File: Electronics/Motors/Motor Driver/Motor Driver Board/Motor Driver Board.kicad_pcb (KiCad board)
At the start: 4 copper layers, 102 x 75 mm, 158 parts, among them IC201 TPS563202DRLR, IC202 TPS563202DRLR, IC301 TJA1057GT/3, IC302 STM32H723ZGT6, J201 Conn_01x02_Pin, J202 Screw_Terminal_01x02, J203 Conn_01x02_Pin, J204 Conn_01x02_Pin, J301 TC2030, J302 Screw_Terminal_01x03, J303 TYPE-C-31-M-12, J401 XT60PW-F, J402 XT60PW-F, J403 XT60PW-M, J404 XT60PW-F, J405 XT60-M-Vertical, J406 Conn_01x05, J407 Conn_01x05, J408 Conn_01x05, Q201 DMP3028LFDE, SW301 SW_DIP_x02, T401 NVMFS4C05NT1G, T402 NVMFS4C05NT1G, T403 NVMFS4C05NT1G, T404 NVMFS4C05NT1G, T405 NVMFS4C05NT1G, T406 NVMFS4C05NT1G, T407 NVMFS4C05NT1G, T408 NVMFS4C05NT1G, T409 NVMFS4C05NT1G, T410 NVMFS4C05NT1G, T411 NVMFS4C05NT1G, T412 NVMFS4C05NT1G, U302 LSM6DS3, U303 USBLC6-4SC6-ES, U401 DRV8701ERGER, U402 DRV8701ERGER, U403 DRV8701ERGER, X301 25MHz_Clock, X302 32.768kHz_Clock

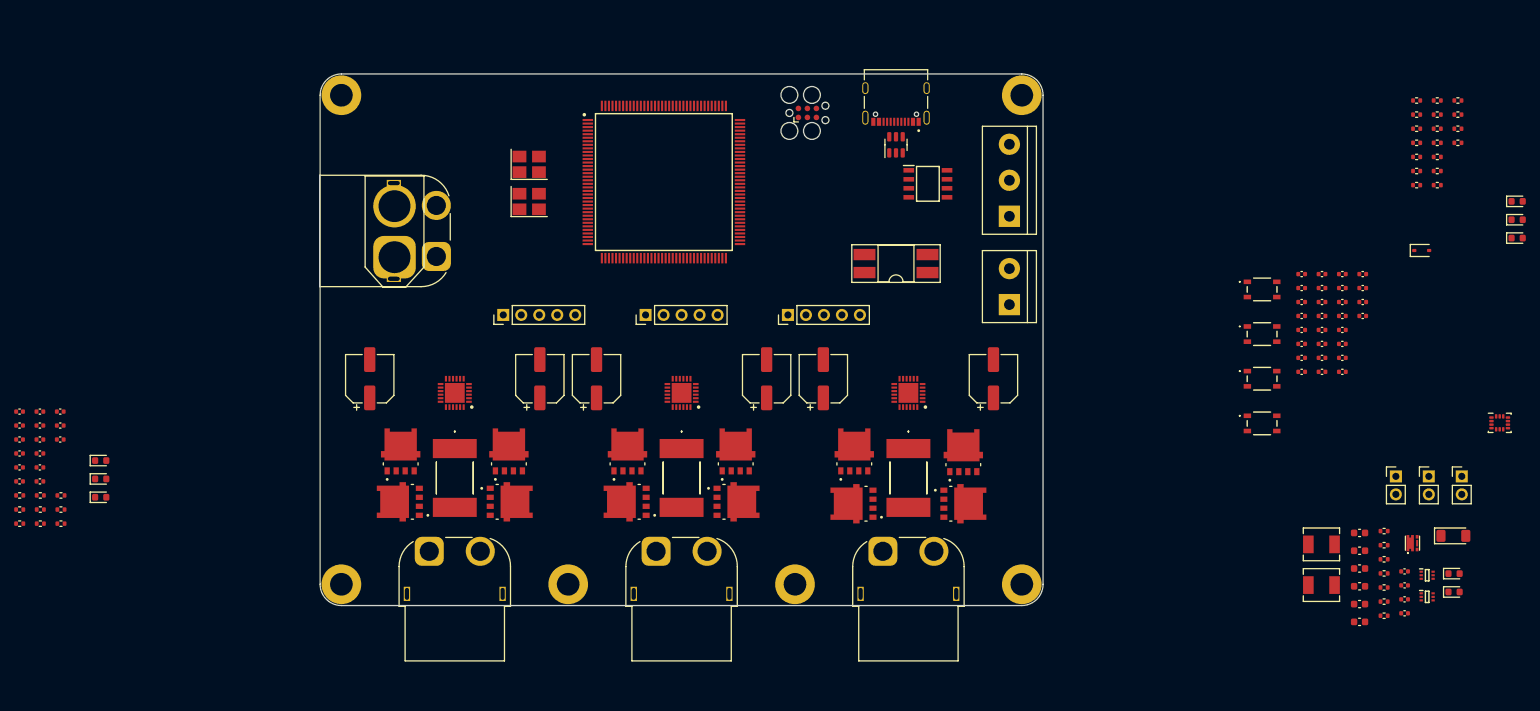
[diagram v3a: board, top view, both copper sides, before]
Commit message: Gateway board layout complete and routing begun
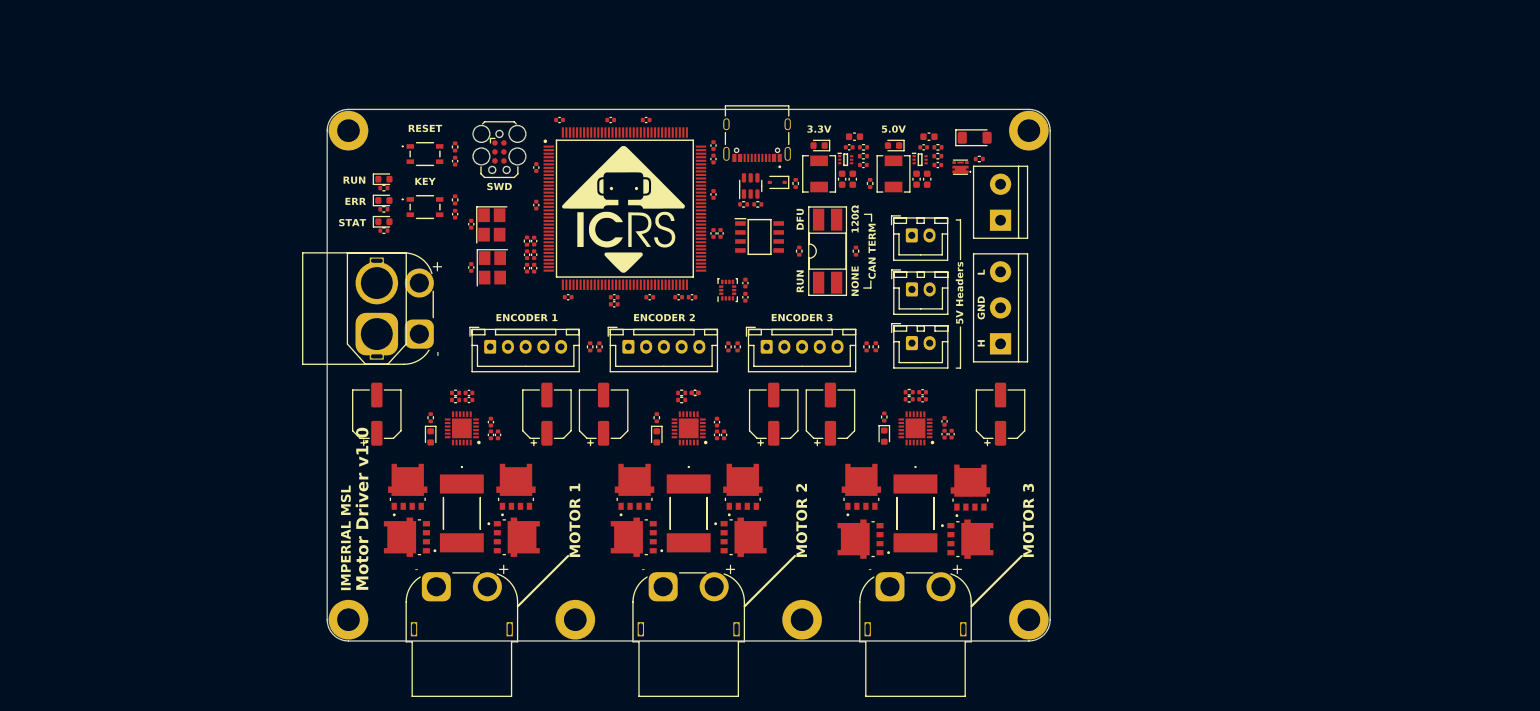
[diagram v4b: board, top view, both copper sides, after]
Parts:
- removed C305: 10n, Capacitor_SMD:C_0402_1005Metric
- removed J408: Conn_01x05, Connector_PinHeader_2.54mm:PinHeader_1x05_P2.54mm_Vertical
- removed R305, R306: 10k, Resistor_SMD:R_0402_1005Metric
- removed S302, S303: TS20-42-25-WT-160-SMT-TR, MSL Footprints:TS204225WT160SMTTRMSL
- added G***: LOGO, MSL Footprints:ICRS_20mm, F.Cu at (142.0, 74.0)
- added G***: LOGO, MSL Footprints:ICRS_50mm, B.Cu at (151.0, 95.0)
- added J409: JST_2.5mm_1x5, Connector_JST:JST_XH_B5B-XH-A_1x05_P2.50mm_Vertical, F.Cu at (142.5, 93.5)
- added REF**: ESD-Logo_8.9x8mm_SilkScreen, Symbol:ESD-Logo_8.9x8mm_SilkScreen, B.Cu at (124.5, 116.0)
- added REF**: WEEE-Logo_5.6x8mm_SilkScreen, Symbol:WEEE-Logo_5.6x8mm_SilkScreen, B.Cu at (113.9, 115.8)
- C304: value 10n -> 100n
- J201, J203, J204: value Conn_01x02_Pin -> JST-XH-2.50mm; footprint Connector_PinHeader_2.54mm:PinHeader_1x02_P2.54mm_Vertical -> Connector_JST:JST_XH_B2B-XH-A_1x02_P2.50mm_Vertical
- J202: value Screw_Terminal_01x02 -> Pluggable_Terminal_01x02; footprint TerminalBlock:TerminalBlock_bornier-2_P5.08mm -> MSL Footprints:Pluggable_terminal-2_P5.08mm
- J301: footprint Connector:Tag-Connect_TC2030-IDC-FP_2x03_P1.27mm_Vertical -> MSL Footprints:Tag-Connect_TC2030-IDC-FP_2x03_P1.27mm_Vertical
- J302: value Screw_Terminal_01x03 -> Pluggable_Terminal_01x03; footprint TerminalBlock:TerminalBlock_bornier-3_P5.08mm -> MSL Footprints:Pluggable_terminal-3_P5.08mm
- J406, J407: value Conn_01x05 -> JST_2.5mm_1x5; footprint Connector_PinHeader_2.54mm:PinHeader_1x05_P2.54mm_Vertical -> Connector_JST:JST_XH_B5B-XH-A_1x05_P2.50mm_Vertical
- R201: value 330R -> 4k7
- moved D302 160.0 mm to (108.0, 69.8)
- moved D303 159.9 mm to (108.0, 75.8)
- moved D301 159.9 mm to (108.0, 72.8)
- moved R301 146.3 mm to (108.0, 74.1), turned to 180 degrees
- moved R303 146.2 mm to (108.0, 77.1), turned to 180 degrees
- moved R302 145.9 mm to (108.0, 71.1), turned to 180 degrees
- moved R317 141.5 mm to (118.0, 65.3), turned to 90 degrees
- moved R304 135.8 mm to (118.0, 72.8), turned to 90 degrees
- moved C405 130.7 mm to (187.1, 104.0), turned to -90 degrees
- moved C328 129.9 mm to (118.0, 67.3), turned to -90 degrees
- moved C412 128.7 mm to (188.1, 105.8), turned to 90 degrees
- moved C407 127.7 mm to (187.1, 105.8), turned to 90 degrees
- moved C403 127.6 mm to (184.0, 99.9)
- moved C401 127.4 mm to (184.0, 100.9)
- moved FB301 127.1 mm to (128.2, 78.6), turned to -90 degrees
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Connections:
- net BTN1 renamed BTN
- net Net-(IC302-VDDA) renamed /Microcontroller/VDDA
- C304 pad 1: BTN2 -> +3V3
- D202 pad 1: /Power/5V_LED_K -> GND
- D202 pad 2: +5V -> /Power/5V_LED_A
- D203 pad 1: /Power/3V3_LED_K -> GND
- D203 pad 2: +3.3V -> /Power/3V3_LED_A
- IC302 pad 10: SDA2 -> unconnected-(IC302-PF0-Pad10)
- IC302 pad 11: SCL2 -> unconnected-(IC302-PF1-Pad11)
- IC302 pad 123: MOSI -> unconnected-(IC302-PD7-Pad123)
- IC302 pad 124: MISO -> unconnected-(IC302-PG9-Pad124)
- IC302 pad 125: CS -> unconnected-(IC302-PG10-Pad125)
- IC302 pad 126: SCK -> unconnected-(IC302-PG11-Pad126)
- IC302 pad 136: SCL1 -> unconnected-(IC302-PB6-Pad136)
- IC302 pad 137: SDA1 -> unconnected-(IC302-PB7-Pad137)
- IC302 pad 54: unconnected-(IC302-PF14-Pad54) -> SCL4
- IC302 pad 55: unconnected-(IC302-PF15-Pad55) -> SDA4
- IC302 pad 64: unconnected-(IC302-PE11-Pad64) -> CS
- IC302 pad 65: unconnected-(IC302-PE12-Pad65) -> SCK
- IC302 pad 66: unconnected-(IC302-PE13-Pad66) -> MISO
- IC302 pad 67: unconnected-(IC302-PE14-Pad67) -> MOSI
- IC302 pad 69: unconnected-(IC302-PB10-Pad69) -> SCL2
- IC302 pad 70: unconnected-(IC302-PB11-Pad70) -> SDA2
- J302 pad 1: /Microcontroller/CANL -> /Microcontroller/CANH
- J302 pad 3: /Microcontroller/CANH -> /Microcontroller/CANL
- J406 pad 2: SDA1 -> SDA2
- J406 pad 3: SCL1 -> SCL2
- J407 pad 2: SDA2 -> SDA3
- J407 pad 3: SCL2 -> SCL3
- Q201 pad 8: (no net) -> VIN_RAW
- R206 pad 1: /Power/5V_LED_K -> +5V
- R206 pad 2: GND -> /Power/5V_LED_A
- R207 pad 1: /Power/3V3_LED_K -> +3.3V
- R207 pad 2: GND -> /Power/3V3_LED_A
- R312 pad 2: SCL1 -> SCL4
- R314 pad 2: SDA1 -> SDA4
- SW301 pad 1: /Microcontroller/CAN_SW -> +3V3
- SW301 pad 2: +3V3 -> /Microcontroller/CAN_SW
- SW301 pad 3: BOOT0 -> /Microcontroller/CANH
- SW301 pad 4: /Microcontroller/CANH -> BOOT0
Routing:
- net GND: track 0.00 -> 52.0 mm
- added copper zone on In1.Cu, net GND
- added copper zone on In2.Cu, net GND
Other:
- board text added: "120Ω"
- board text added: "3.3V"
- board text added: "5.0V"
- board text added: "5V"
- board text added: "5V Headers"
- board text added: "CAN TERM"
- board text added: "DFU"
- board text added: "Designed by Ben Smith 2023"
- board text added: "ENCODER 1"
- board text added: "ENCODER 2"
- board text added: "ENCODER 3"
- board text added: "ERR"
- board text added: "FD-CAN"
- board text added: "GND"
- board text added: "H"
- board text added: "KEY"
- board text added: "L"
- board text added: "MOTOR 1"
- board text added: "MOTOR 2"
- board text added: "MOTOR 3"
- board text added: "NONE"
- board text added: "RESET"
- board text added: "RUN"
- board text added: "STAT"
- board text added: "SWD"
- board text added: "_{IMPERIAL MSL} Motor Driver v1.0"

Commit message: Sensor hub board done
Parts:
- removed REF**: ESD-Logo_8.9x8mm_SilkScreen, Symbol:ESD-Logo_8.9x8mm_SilkScreen
- removed REF**: WEEE-Logo_5.6x8mm_SilkScreen, Symbol:WEEE-Logo_5.6x8mm_SilkScreen
- added G***: LOGO, MSL Footprints:DC_logo_4mm, B.Cu at (199.0, 85.5)
- added G***: LOGO, MSL Footprints:DC_logo_4mm, B.Cu at (117.6, 83.0)
- moved D402 105.0 mm to (219.5, 102.1)
- moved R402 105.0 mm to (219.5, 99.4)
- moved R404 101.4 mm to (219.4, 96.7)
- moved R406 101.4 mm to (219.4, 95.7)
- moved D403 79.2 mm to (225.6, 102.1)
- moved R409 79.2 mm to (225.6, 99.4)
- moved R410 76.1 mm to (225.9, 95.9)
- moved R411 76.0 mm to (225.9, 96.9)
- moved R315 69.6 mm to (224.9, 106.7)
- moved R316 69.6 mm to (226.2, 106.7)
- moved D401 54.8 mm to (233.2, 101.9)
- moved R401 54.8 mm to (233.2, 99.2)
- moved R403 51.1 mm to (233.0, 96.8)
- moved R405 51.1 mm to (233.0, 95.8)
- moved R308 35.1 mm to (136.8, 61.5), turned to 0 degrees
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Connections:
- C301 pad 1: +3V3 -> +3.3V
- C302 pad 2: +3V3 -> +3.3V
- C304 pad 1: +3V3 -> +3.3V
- C308 pad 1: +3V3 -> +3.3V
- C310 pad 1: +3V3 -> +3.3V
- C312 pad 1: +3V3 -> +3.3V
- C313 pad 1: +3V3 -> +3.3V
- C314 pad 1: +3V3 -> +3.3V
- C315 pad 1: +3V3 -> +3.3V
- C316 pad 1: +3V3 -> +3.3V
- C317 pad 1: +3V3 -> +3.3V
- C318 pad 1: +3V3 -> +3.3V
- C319 pad 1: +3V3 -> +3.3V
- C320 pad 1: +3V3 -> +3.3V
- C322 pad 1: +3V3 -> +3.3V
- C323 pad 1: +3V3 -> +3.3V
- C324 pad 1: +3V3 -> +3.3V
- C326 pad 1: +3V3 -> +3.3V
- C327 pad 1: +3V3 -> +3.3V
- FB301 pad 2: +3V3 -> +3.3V
- IC301 pad 5: +3V3 -> +3.3V
- IC302 pad 108: +3V3 -> +3.3V
- IC302 pad 121: +3V3 -> +3.3V
- IC302 pad 131: +3V3 -> +3.3V
- IC302 pad 143: +3V3 -> +3.3V
- IC302 pad 144: +3V3 -> +3.3V
- IC302 pad 17: +3V3 -> +3.3V
- IC302 pad 30: +3V3 -> +3.3V
- IC302 pad 34: unconnected-(IC302-PA0-Pad34) -> M1_PH
- IC302 pad 35: unconnected-(IC302-PA1-Pad35) -> M1_EN
- IC302 pad 36: unconnected-(IC302-PA2-Pad36) -> M1_NSLEEP
- IC302 pad 37: unconnected-(IC302-PA3-Pad37) -> M1_NFAULT
- IC302 pad 39: +3V3 -> +3.3V
- IC302 pad 41: unconnected-(IC302-PA5-Pad41) -> M1_SNSOUT
- IC302 pad 42: unconnected-(IC302-PA6-Pad42) -> M1_SO
- IC302 pad 46: unconnected-(IC302-PB0-Pad46) -> M2_SO
- IC302 pad 49: unconnected-(IC302-PF11-Pad49) -> M3_SO
- IC302 pad 52: +3V3 -> +3.3V
- IC302 pad 6: +3V3 -> +3.3V
- IC302 pad 60: unconnected-(IC302-PE9-Pad60) -> M2_PH
- IC302 pad 62: +3V3 -> +3.3V
- IC302 pad 64: CS -> M2_EN
- IC302 pad 65: SCK -> M2_NSLEEP
- IC302 pad 66: MISO -> unconnected-(IC302-PE13-Pad66)
- IC302 pad 67: MOSI -> unconnected-(IC302-PE14-Pad67)
- IC302 pad 72: +3V3 -> +3.3V
- IC302 pad 73: unconnected-(IC302-PB12-Pad73) -> M2_SNSOUT
- IC302 pad 74: unconnected-(IC302-PB13-Pad74) -> M2_NFAULT
- IC302 pad 75: unconnected-(IC302-PB14-Pad75) -> M3_PH
- IC302 pad 76: unconnected-(IC302-PB15-Pad76) -> M3_EN
- IC302 pad 77: unconnected-(IC302-PD8-Pad77) -> M3_NSLEEP
- IC302 pad 78: unconnected-(IC302-PD9-Pad78) -> M3_SNSOUT
- IC302 pad 79: unconnected-(IC302-PD10-Pad79) -> M3_NFAULT
- IC302 pad 84: +3V3 -> +3.3V
- IC302 pad 95: +3V3 -> +3.3V
- J301 pad 1: +3V3 -> +3.3V
- J406 pad 5: +3V3 -> +3.3V
- J407 pad 5: +3V3 -> +3.3V
- J409 pad 5: +3V3 -> +3.3V
- R304 pad 2: +3V3 -> +3.3V
- R311 pad 1: +3V3 -> +3.3V
- R312 pad 1: +3V3 -> +3.3V
- R313 pad 1: +3V3 -> +3.3V
- R314 pad 1: +3V3 -> +3.3V
- R315 pad 1: +3V3 -> +3.3V
- R316 pad 1: +3V3 -> +3.3V
- R317 pad 2: +3V3 -> +3.3V
- R403 pad 1: /Motor Drivers/M3_DVDD -> +3.3V
- R404 pad 1: /Motor Drivers/M1_DVDD -> +3.3V
- R405 pad 1: /Motor Drivers/M3_DVDD -> +3.3V
- R406 pad 1: /Motor Drivers/M1_DVDD -> +3.3V
- R410 pad 1: /Motor Drivers/M2_DVDD -> +3.3V
- R411 pad 1: /Motor Drivers/M2_DVDD -> +3.3V
- SW301 pad 1: +3V3 -> +3.3V
- U302 pad 5: +3V3 -> +3.3V
- U302 pad 8: +3V3 -> +3.3V
- U303 pad 1: /Microcontroller/CC1 -> /Microcontroller/CC2
- U303 pad 3: /Microcontroller/CC2 -> /Microcontroller/CC1
- U303 pad 4: USB_DP -> USB_DN
- U303 pad 6: USB_DN -> USB_DP
- X301 pad 4: +3V3 -> +3.3V
- X302 pad 4: +3V3 -> +3.3V
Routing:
- net +3.3V: track 0.00 -> 65.0 mm, vias 0 -> 21
- net M3_SO: track 0.00 -> 56.6 mm, vias 0 -> 2
- net M3_NFAULT: track 0.00 -> 46.2 mm, vias 0 -> 2
- net M3_SNSOUT: track 0.00 -> 45.9 mm
- net M3_PH: track 0.00 -> 44.2 mm
- net M3_NSLEEP: track 0.00 -> 44.2 mm
- net M3_EN: track 0.00 -> 44.2 mm
- net M1_PH: track 0.00 -> 34.0 mm
- net M1_SO: track 0.00 -> 33.8 mm
- net SCL3: track 0.00 -> 33.5 mm
- net SDA3: track 0.00 -> 32.5 mm
- net M1_EN: track 0.00 -> 32.4 mm
- net SWDIO: track 0.00 -> 32.0 mm
- net M1_SNSOUT: track 0.00 -> 31.7 mm
- net VMOT: track 0.00 -> 31.1 mm, vias 0 -> 96
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- added copper zone on B.Cu, net /Motor Drivers/M1_OUT_A
- added copper zone on F.Cu, net /Motor Drivers/M1_OUT_A
- added copper zone on B.Cu, net /Motor Drivers/M1_OUT_B
- added copper zone on F.Cu, net /Motor Drivers/M1_OUT_B
- added copper zone on F.Cu, net /Motor Drivers/M1_SP
- added copper zone on B.Cu, net /Motor Drivers/M2_OUT_A
- added copper zone on F.Cu, net /Motor Drivers/M2_OUT_A
- added copper zone on B.Cu, net /Motor Drivers/M2_OUT_B
- added copper zone on F.Cu, net /Motor Drivers/M2_OUT_B
- added copper zone on F.Cu, net /Motor Drivers/M2_SP
- added copper zone on B.Cu, net /Motor Drivers/M3_OUT_A
- added copper zone on F.Cu, net /Motor Drivers/M3_OUT_A
- added copper zone on B.Cu, net /Motor Drivers/M3_OUT_B
- added copper zone on F.Cu, net /Motor Drivers/M3_OUT_B
- added copper zone on F.Cu, net /Motor Drivers/M3_SP
- added copper zone on F.Cu, net GND
- added copper zone on B.Cu, net VMOT
- added copper zone on F.Cu, net VMOT
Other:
- board text added: "+"
- board text added: "-"
- board text added: "Input: 12-24V 30A"
- board text added: "Input: 5-16V 0.5A"
- board text added: "locked"
- board text removed: "ENCODER 1"
- board text removed: "ENCODER 2"
- board text removed: "ENCODER 3"
- board text removed: "MOTOR 1"
- board text removed: "MOTOR 2"
- board text removed: "MOTOR 3"
- board text removed: "_{IMPERIAL MSL} Motor Driver v1.0"
